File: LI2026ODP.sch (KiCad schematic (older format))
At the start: 33 parts, among them J1 9-1437539-2, J2 Conn_01x05_Male, U1 LM2936MM-3.3, U2 STM32G0B1KET6, U3 max6921aui

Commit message: Update C1 from 1608 to 2012
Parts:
- removed C1: 4.7u, Capacitor_SMD:C_0603_1608Metric_Pad1.08x0.95mm_HandSolder, symbol Device:C
- added C1: 22uF, Capacitor_Tantalum_SMD:CP_EIA-3216-10_Kemet-I_Pad1.58x1.35mm_HandSolder, symbol Device:CP
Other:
- note added: "See data sheet of LM2936MM-3.3 for ESR of C1: \n8ohm > ESR >= 300mohm"
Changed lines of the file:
@@
-$EndComp
-$Comp
-L Device:C C1
-U 1 1 61F87BB0
-P 2850 5700
-F 0 "C1" H 2965 5746 50  0000 L CNN
-F 1 "4.7u" H 2965 5655 50  0000 L CNN
-F 2 "Capacitor_SMD:C_0603_1608Metric_Pad1.08x0.95mm_HandSolder" H 2888 5550 50  0001 C CNN
-F 3 "~" H 2850 5700 50  0001 C CNN
-	1    2850 5700
-	1    0    0    -1
 $EndComp
 $Comp
@@
 Wire Wire Line
 	1050 6950 1050 7050
+$Comp
+L Device:CP C1
+U 1 1 61E33765
+P 2850 5700
+F 0 "C1" H 2968 5746 50  0000 L CNN
+F 1 "22uF" H 2968 5655 50  0000 L CNN
+F 2 "Capacitor_Tantalum_SMD:CP_EIA-3216-10_Kemet-I_Pad1.58x1.35mm_HandSolder" H 2888 5550 50  0001 C CNN
+F 3 "~" H 2850 5700 50  0001 C CNN
+	1    2850 5700
+	1    0    0    -1
+$EndComp
+Text Notes 1150 7650 0    50   ~ 0
+See data sheet of LM2936MM-3.3 for ESR of C1: \n8ohm > ESR >= 300mohm
 $EndSCHEMATC

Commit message: Add capacitor to NRST for noise protection.
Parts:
- added C5: 0.1u, Capacitor_SMD:C_0603_1608Metric_Pad1.08x0.95mm_HandSolder, symbol Device:C
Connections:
- wire segments 142 -> 145
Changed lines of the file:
@@
 $EndComp
 Wire Wire Line
-	1650 4200 1250 4200
+	1650 4200 1350 4200
 Wire Wire Line
 	5050 2500 4650 2500
@@
 Text Notes 1150 7650 0    50   ~ 0
 See data sheet of LM2936MM-3.3 for ESR of C1: \n8ohm > ESR >= 300mohm
+$Comp
+L Device:C C5
+U 1 1 61ECB9EB
+P 1350 4400
+F 0 "C5" H 1465 4446 50  0000 L CNN
+F 1 "0.1u" H 1465 4355 50  0000 L CNN
+F 2 "Capacitor_SMD:C_0603_1608Metric_Pad1.08x0.95mm_HandSolder" H 1388 4250 50  0001 C CNN
+F 3 "~" H 1350 4400 50  0001 C CNN
+	1    1350 4400
+	1    0    0    -1
+$EndComp
+Wire Wire Line
+	1350 4250 1350 4200
+$Comp
+L power:GND #PWR03
+U 1 1 61ECB9F2
+P 1350 4700
+F 0 "#PWR03" H 1350 4450 50  0001 C CNN
+F 1 "GND" H 1355 4527 50  0000 C CNN
+F 2 "" H 1350 4700 50  0001 C CNN
+F 3 "" H 1350 4700 50  0001 C CNN
+	1    1350 4700
+	1    0    0    -1
+$EndComp
+Wire Wire Line
+	1350 4700 1350 4550
+Connection ~ 1350 4200
+Wire Wire Line
+	1350 4200 1250 4200
 $EndSCHEMATC

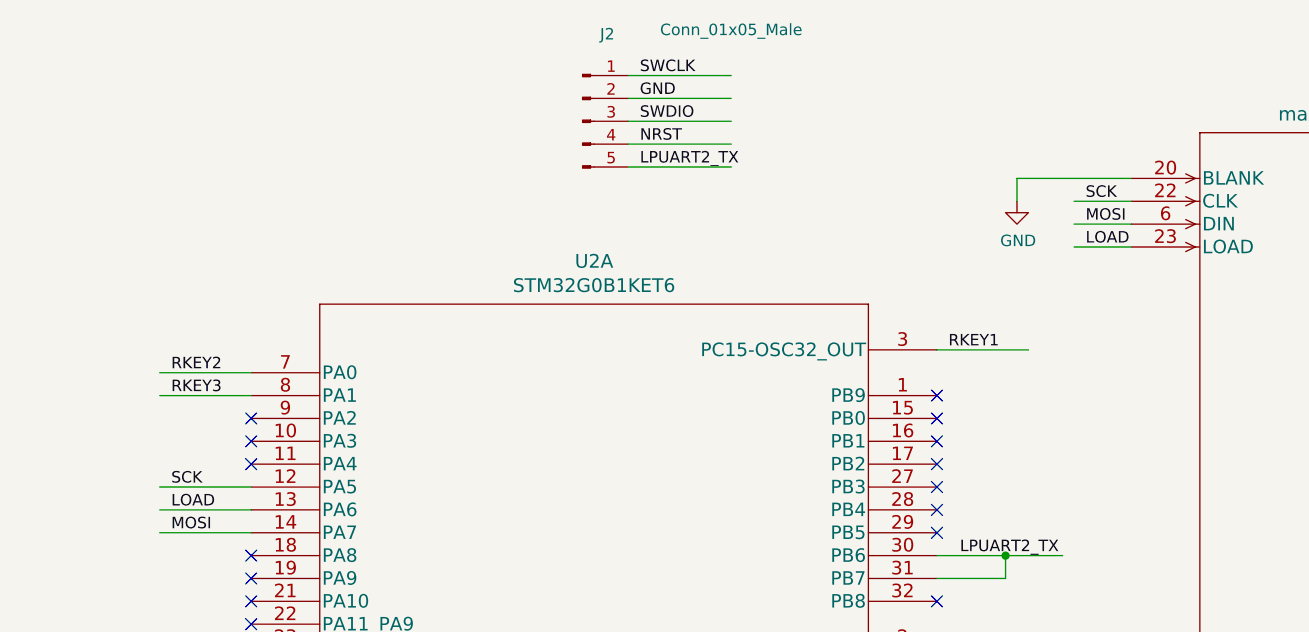
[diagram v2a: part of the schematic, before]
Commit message: Change BLANK control of MAX6921
from the hardwired to the software control.
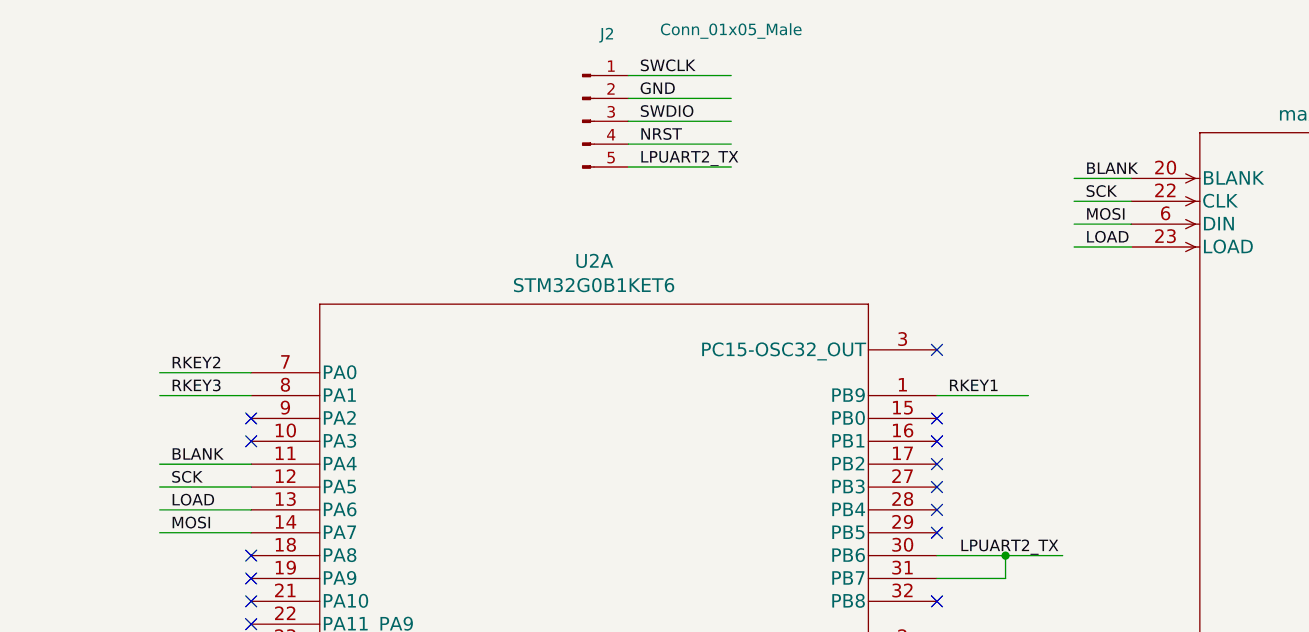
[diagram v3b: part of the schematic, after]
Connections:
- net labels added: BLANK
- no-connect marks 34 -> 33
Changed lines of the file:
@@
 	1650 4200 1350 4200
 Wire Wire Line
-	5050 2500 4650 2500
+	5050 2700 4650 2700
 Wire Wire Line
 	1650 3100 1250 3100
@@
 NoConn ~ 7300 3050
 NoConn ~ 1650 2800
-NoConn ~ 4650 2700
+NoConn ~ 4650 2500
 NoConn ~ 4650 2800
 NoConn ~ 4650 2900
@@
 NoConn ~ 4650 3900
 NoConn ~ 1650 2900
-NoConn ~ 1650 3000
 NoConn ~ 1650 3400
 NoConn ~ 1650 3500
@@
 Text Label 3350 1700 0    50   ~ 0
 LPUART2_TX
-Text Label 4700 2500 0    50   ~ 0
+Text Label 4700 2700 0    50   ~ 0
 RKEY1
 Wire Wire Line
@@
 Text Notes 1850 4600 0    50   ~ 0
 PB7 is LPUART2_RX. This signal is not used. So, tied with TX.
-$Comp
-L power:GND #PWR0102
-U 1 1 61E39126
-P 5000 1850
-F 0 "#PWR0102" H 5000 1600 50  0001 C CNN
-F 1 "GND" H 5005 1677 50  0000 C CNN
-F 2 "" H 5000 1850 50  0001 C CNN
-F 3 "" H 5000 1850 50  0001 C CNN
-	1    5000 1850
-	1    0    0    -1
-$EndComp
-Wire Wire Line
-	5000 1750 5000 1850
-Wire Wire Line
-	5000 1750 5500 1750
+Wire Wire Line
+	5250 1750 5500 1750
 $Comp
 L Device:C C4
@@
 Wire Wire Line
 	1350 4200 1250 4200
+Text Label 5300 1750 0    50   ~ 0
+BLANK
+Wire Wire Line
+	1650 3000 1250 3000
+Text Label 1300 3000 0    50   ~ 0
+BLANK
 $EndSCHEMATC
